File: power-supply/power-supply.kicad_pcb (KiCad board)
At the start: 2 copper layers, 200 x 140 mm, 34 parts, among them J101 CUI_PD-30, T101 Transformer_1P_2S, U401 LM7815_TO220, U402 LM7915_TO220

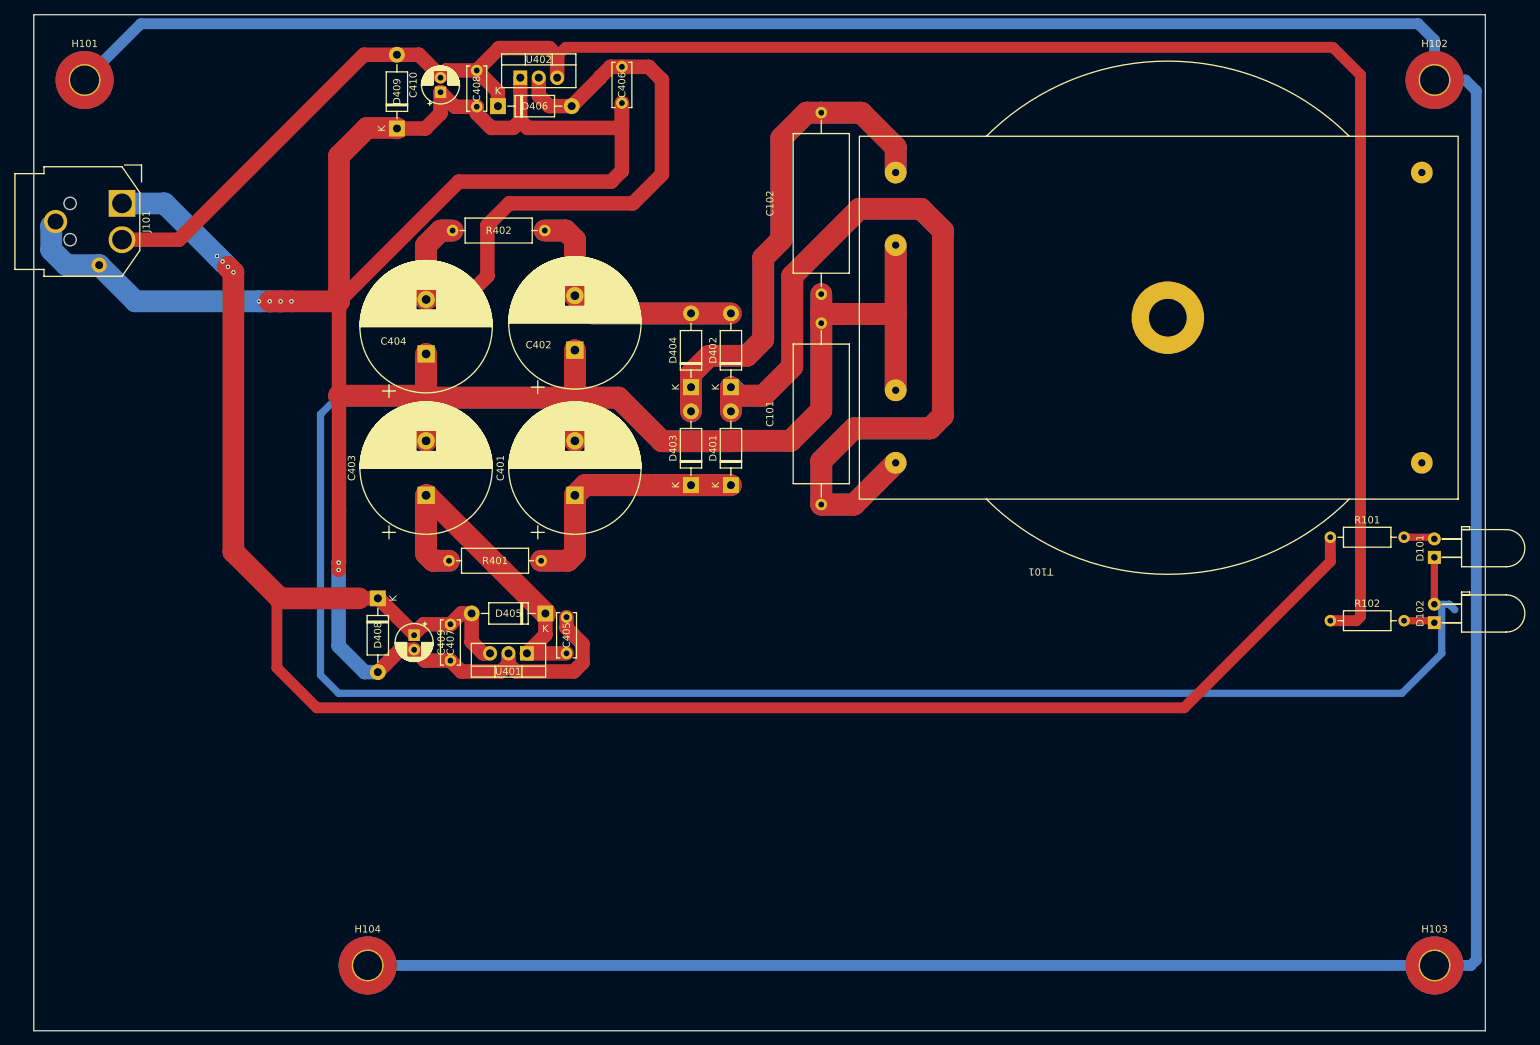
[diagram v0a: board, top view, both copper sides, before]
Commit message: Some additions to power supply
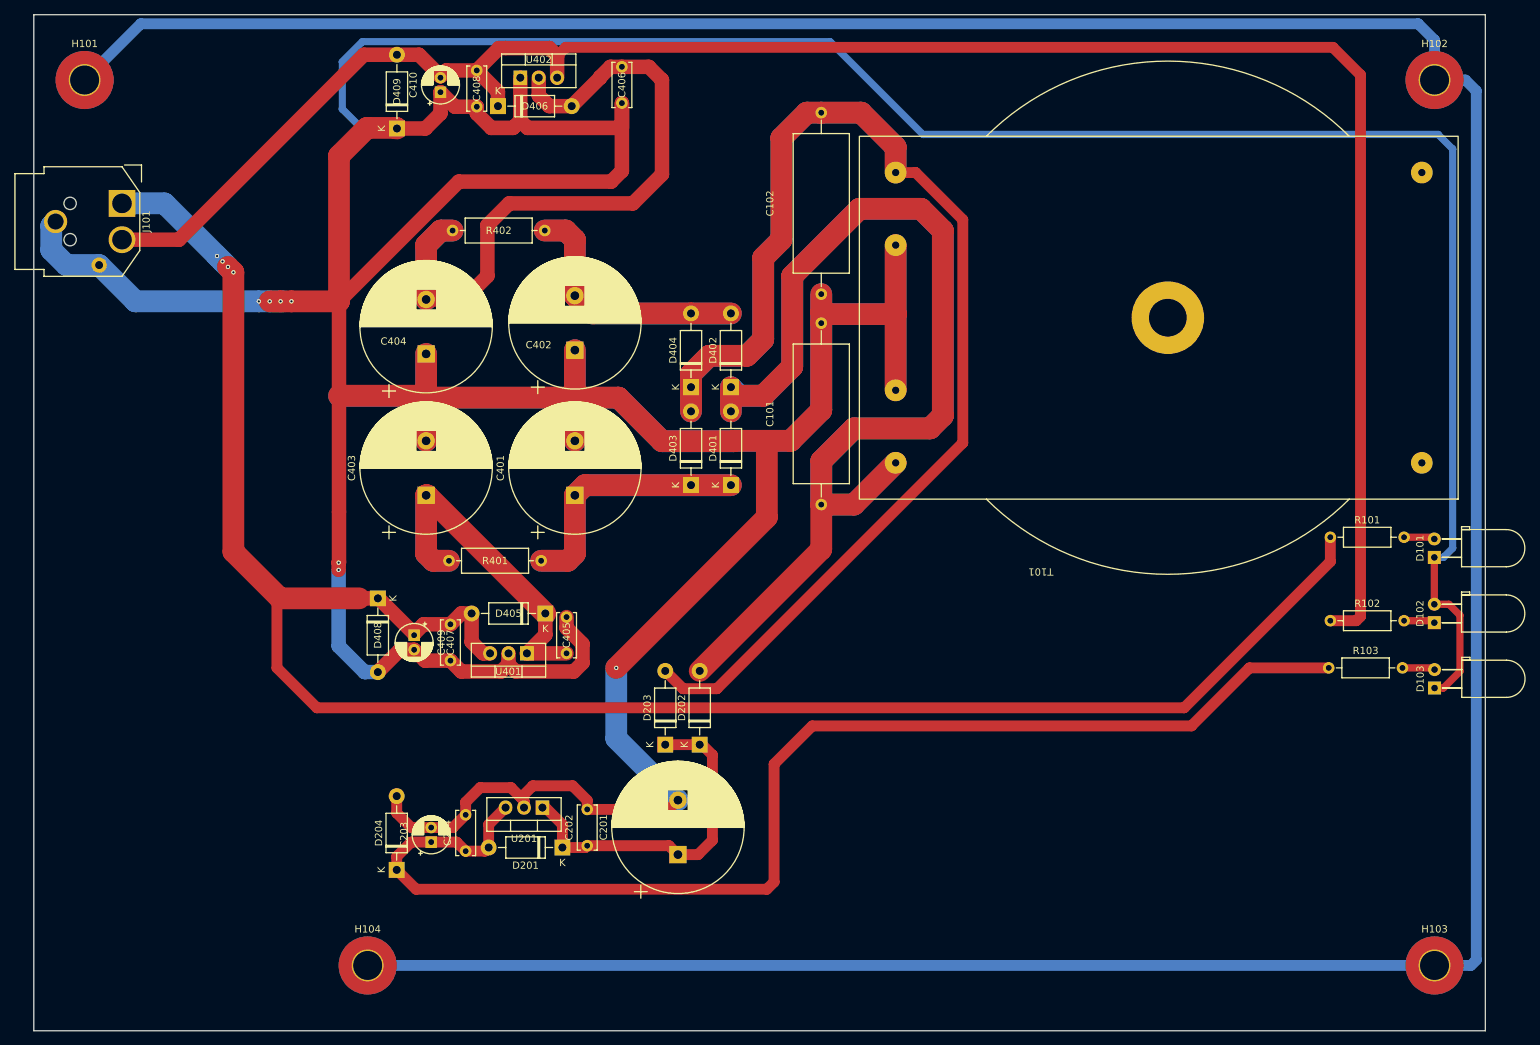
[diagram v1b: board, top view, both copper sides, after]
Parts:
- added C201: 2200u, Capacitor_THT:CP_Radial_D18.0mm_P7.50mm, F.Cu at (117.8, 138.7)
- added C202: 100n, Capacitor_THT:C_Disc_D6.0mm_W2.5mm_P5.00mm, F.Cu at (105.2, 137.5)
- added C203: 10u, Capacitor_THT:CP_Radial_D5.0mm_P2.00mm, F.Cu at (83.8, 137.0)
- added C204: 100n, Capacitor_THT:C_Disc_D6.0mm_W2.5mm_P5.00mm, F.Cu at (88.5, 138.2)
- added D103: LED, LED_THT:LED_D5.0mm_Horizontal_O3.81mm_Z3.0mm, F.Cu at (222.0, 115.8)
- added D201: 1N4004, Diode_THT:D_DO-41_SOD81_P10.16mm_Horizontal, F.Cu at (101.8, 137.8)
- added D202: 1N4004, Diode_THT:D_DO-41_SOD81_P10.16mm_Horizontal, F.Cu at (120.8, 123.6)
- added D203: 1N4004, Diode_THT:D_DO-41_SOD81_P10.16mm_Horizontal, F.Cu at (116.0, 123.6)
- added D204: 1N4004, Diode_THT:D_DO-41_SOD81_P10.16mm_Horizontal, F.Cu at (79.0, 140.8)
- added R103: 2k2, Resistor_THT:R_Axial_DIN0207_L6.3mm_D2.5mm_P10.16mm_Horizontal, F.Cu at (207.4, 113.0)
- added U201: LM7812_TO220, Package_TO_SOT_THT:TO-220-3_Vertical, F.Cu at (99.1, 132.2)
- R101, R102: value 1k -> 2k2
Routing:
- net +12V: track 0.00 -> 174.2 mm
- net GND: track 774.5 -> 931.1 mm, vias 6 -> 7
- net /Voltage regulator/AC2: track 135.9 -> 234.6 mm
- net Net-(D201-K): track 0.00 -> 47.8 mm
- net /Voltage regulator/AC1: track 231.0 -> 260.8 mm
- net Net-(D103-A): track 0.00 -> 4.52 mm
